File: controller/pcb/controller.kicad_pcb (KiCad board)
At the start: 2 copper layers, 108.1 x 143.5 mm, 75 parts, among them J1 POWER, J2 10K POT, Q1 2N2222, Q10 2N2222, Q11 2N2222, Q12 TIP41, Q13 TIP41, Q14 2N2907, Q15 2N2222, Q2 TIP42, Q3 TIP42, Q4 2N2222, Q5 2N2222, Q6 2N2222, Q7 2N2222, Q8 2N2222, Q9 2N2222, U1 LM78M05_TO220, U2 PIC12F1501-ISN, U3 74HC595

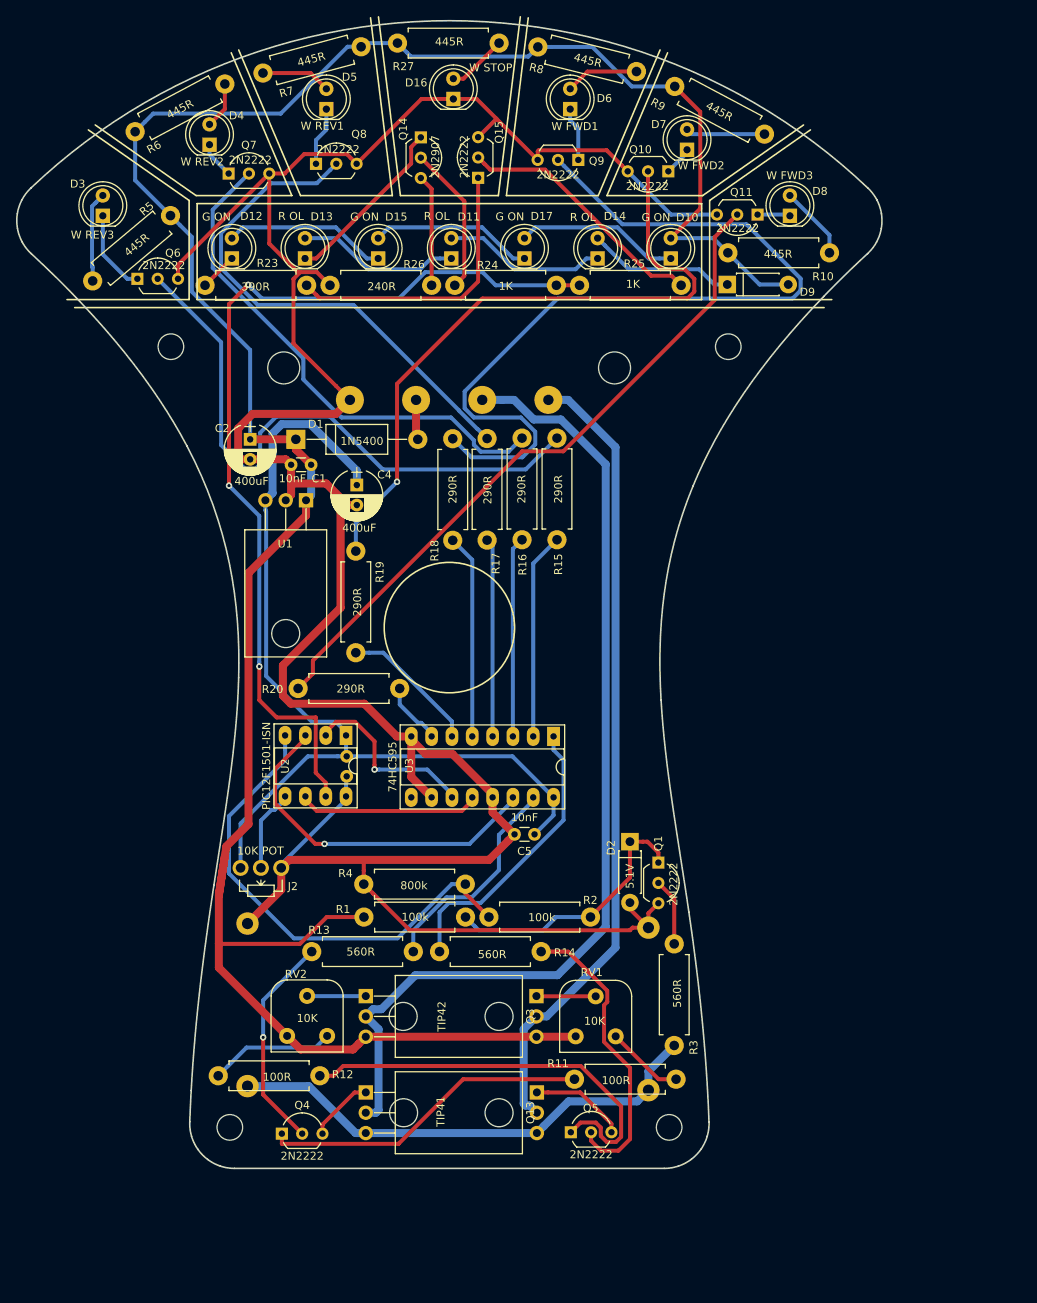
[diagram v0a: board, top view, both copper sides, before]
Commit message: Added gradient control to PCB.
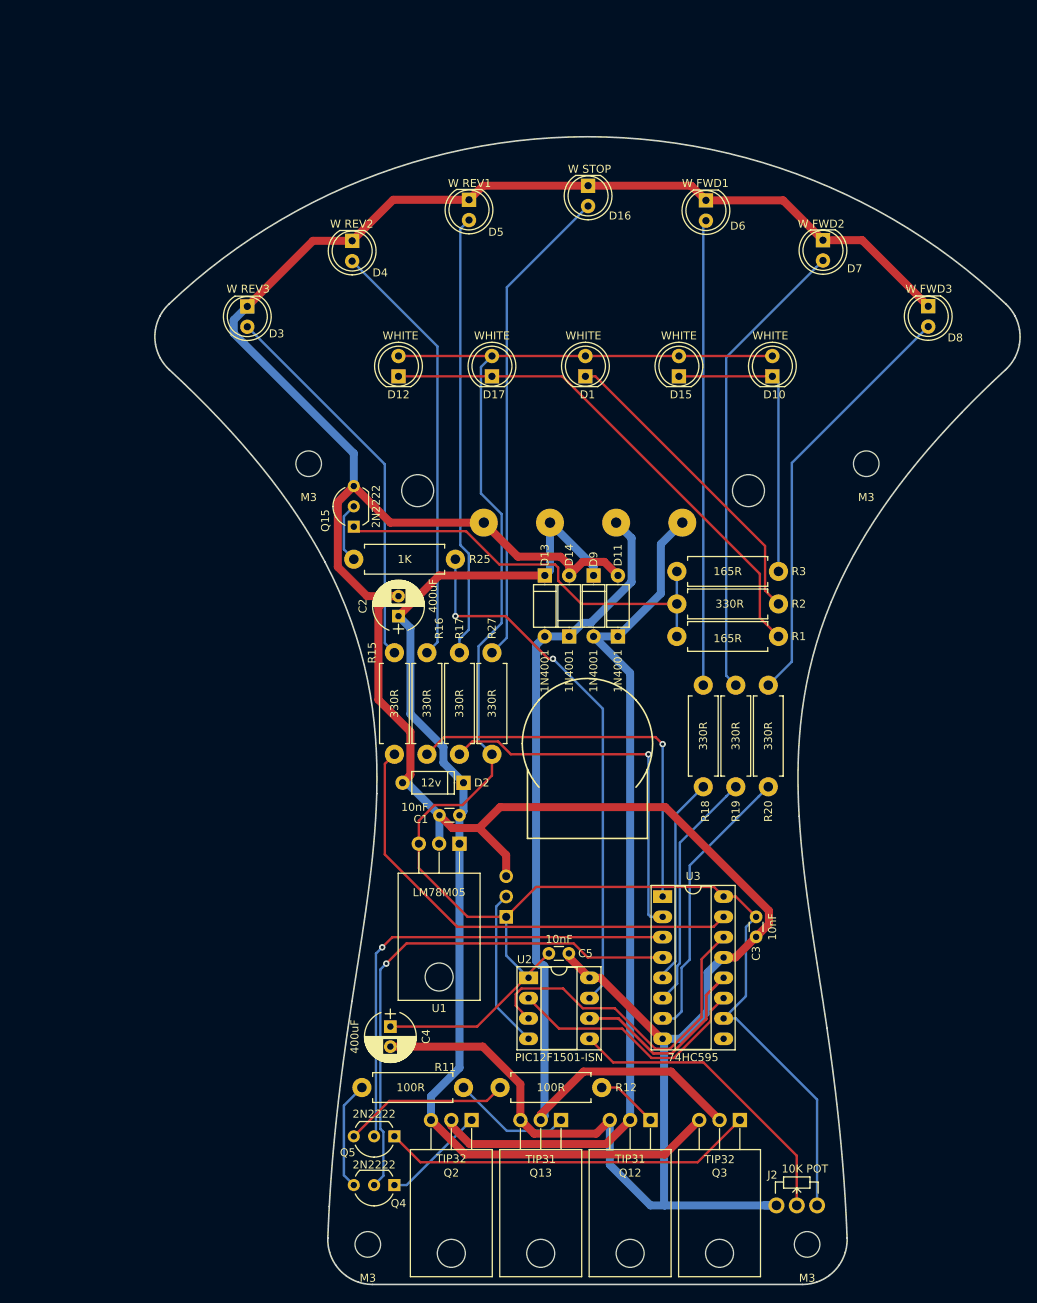
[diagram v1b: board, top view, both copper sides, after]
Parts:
- removed Q1, Q10, Q11, Q6, Q7, Q8, Q9: 2N2222, TO_SOT_Packages_THT:TO-92_Inline_Wide
- removed Q14: 2N2907, TO_SOT_Packages_THT:TO-92_Inline_Wide
- removed R10, R5, R6, R7, R8, R9: 445R, Resistors_THT:R_Axial_DIN0411_L9.9mm_D3.6mm_P12.70mm_Horizontal
- removed R13, R14: 560R, Resistors_THT:R_Axial_DIN0411_L9.9mm_D3.6mm_P12.70mm_Horizontal
- removed R21, R22: 1R, Resistors_THT:R_Axial_DIN0614_L14.3mm_D5.7mm_P20.32mm_Horizontal
- removed R23: 390R, Resistors_THT:R_Axial_DIN0411_L9.9mm_D3.6mm_P12.70mm_Horizontal
- removed R24: 1K, Resistors_THT:R_Axial_DIN0411_L9.9mm_D3.6mm_P12.70mm_Horizontal
- removed R26: 240R, Resistors_THT:R_Axial_DIN0411_L9.9mm_D3.6mm_P12.70mm_Horizontal
- removed R4: 800k, Resistors_THT:R_Axial_DIN0411_L9.9mm_D3.6mm_P12.70mm_Horizontal
- removed the REF** at (101.9, 160.9)
- removed the REF** at (47.0, 160.9)
- removed the REF** at (109.3, 63.3)
- removed the REF** at (39.6, 63.3)
- removed RV1, RV2: 10K, carnivalben:TrimPot_RM065
- added J3: Gradient, Pin_Headers:Pin_Header_Straight_1x03_Pitch2.54mm, B.Cu at (81.5, 134.6)
- added REF**: M3, Mounting_Holes:MountingHole_3.2mm_M3, F.Cu at (119.2, 175.6)
- added REF**: M3, Mounting_Holes:MountingHole_3.2mm_M3, F.Cu at (64.2, 175.6)
- added REF**: M3, Mounting_Holes:MountingHole_3.2mm_M3, F.Cu at (56.8, 78.0)
- added REF**: M3, Mounting_Holes:MountingHole_3.2mm_M3, F.Cu at (126.5, 78.0)
- C3: moved to F.Cu
- D1: value 1N5400 -> WHITE; footprint Diodes_THT:D_DO-15_P15.24mm_Horizontal -> LEDs:LED_D5.0mm
- D10, D12, D15, D17: value G ON -> WHITE
- D11, D13, D14: value R OL -> 1N4001; footprint LEDs:LED_D5.0mm -> Diodes_THT:D_A-405_P7.62mm_Horizontal
- D2: value 5.1V -> 12v; footprint Diodes_THT:D_DO-41_SOD81_P7.62mm_Horizontal -> Diodes_THT:D_A-405_P7.62mm_Horizontal
- D9: value 5.1V -> 1N4001; footprint Diodes_THT:D_DO-41_SOD81_P7.62mm_Horizontal -> Diodes_THT:D_A-405_P7.62mm_Horizontal
- Q12: value TIP41 -> TIP31; moved to F.Cu
- Q13: value TIP41 -> TIP31
- Q2: value TIP42 -> TIP32; moved to F.Cu
- Q3: value TIP42 -> TIP32
- R1: value 100k -> 165R
- R15, R16, R17, R18, R19, R20: value 290R -> 330R
- R2: value 100k -> 330R
- R27: value 445R -> 330R
- R3: value 560R -> 165R
- U1: value LM78M05_TO220 -> LM78M05
- moved R27 76.2 mm to (79.8, 101.6), turned to 270 degrees
- moved J2 74.9 mm to (115.3, 170.7), turned to 90 degrees
- moved C4 67.8 mm to (67.1, 148.3)
- moved R3 60.7 mm to (115.6, 91.4), turned to 180 degrees
- moved R20 58.8 mm to (114.3, 105.7), turned to 270 degrees
- moved C3 55.0 mm to (112.8, 134.6)
- moved R25 53.4 mm to (62.5, 89.9), turned to 0 degrees
- moved R2 53.3 mm to (115.6, 95.5), turned to 180 degrees
- moved R1 52.5 mm to (115.6, 99.6)
- moved D11 51.6 mm to (95.5, 99.6)
- moved R19 50.4 mm to (110.2, 105.7)
- moved D13 49.7 mm to (86.4, 91.9), turned to 270 degrees
- moved Q3 49.3 mm to (110.7, 160.0), turned to 180 degrees
- moved C1 47.6 mm to (75.7, 121.9)
- moved D14 47.4 mm to (89.4, 99.6)
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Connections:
- C1 pad 1: 12vP -> +12V
- C2 pad 1: 12vP -> +12V
- D1 pad 1: 12vP -> Net-(D1-Pad1)
- D1 pad 2: /12v -> 5v
- D10 pad 2: 12vP -> 5v
- D11 pad 1: Net-(D11-Pad1) -> TRACK+
- D11 pad 2: Net-(D11-Pad2) -> GND
- D12 pad 2: Net-(D12-Pad2) -> 5v
- D13 pad 1: Net-(D13-Pad1) -> +12V
- D13 pad 2: Net-(D11-Pad1) -> TRACK-
- D14 pad 1: Net-(D11-Pad2) -> TRACK-
- D14 pad 2: Net-(D14-Pad2) -> GND
- D15 pad 1: Net-(D12-Pad2) -> Net-(D10-Pad1)
- D15 pad 2: Net-(D15-Pad2) -> 5v
- D17 pad 1: Net-(D15-Pad2) -> Net-(D12-Pad1)
- D17 pad 2: Net-(D10-Pad1) -> 5v
- D2 pad 1: Net-(D2-Pad1) -> +12V
- D3 pad 1: Net-(D3-Pad1) -> GND
- D4 pad 1: Net-(D4-Pad1) -> GND
- D5 pad 1: Net-(D5-Pad1) -> GND
- D6 pad 1: Net-(D6-Pad1) -> GND
- D7 pad 1: Net-(D7-Pad1) -> GND
- D8 pad 1: Net-(D8-Pad1) -> GND
- D9 pad 1: Net-(D14-Pad2) -> +12V
- D9 pad 2: 12vP -> TRACK+
- J1 pad 2: /12v -> +12V
- Q12 pad 3: OVERLOAD_DETECT -> GND
- Q13 pad 3: OVERLOAD_DETECT -> GND
- Q2 pad 3: 12vP -> +12V
- Q3 pad 3: 12vP -> +12V
- Q4 pad 1: Net-(Q4-Pad1) -> Net-(Q2-Pad1)
- Q4 pad 3: Net-(Q13-Pad1) -> Net-(Q4-Pad3)
- Q5 pad 1: Net-(Q5-Pad1) -> Net-(Q3-Pad1)
- Q5 pad 3: Net-(Q12-Pad1) -> Net-(Q5-Pad3)
- R1 pad 1: Net-(D2-Pad1) -> Net-(D12-Pad1)
- R1 pad 2: 12vP -> Net-(Q15-Pad1)
- R11 pad 1: Net-(Q4-Pad1) -> Net-(Q13-Pad1)
- R11 pad 2: Net-(R11-Pad2) -> Net-(Q4-Pad3)
- R12 pad 1: Net-(Q5-Pad1) -> Net-(Q12-Pad1)
- R12 pad 2: Net-(R12-Pad2) -> Net-(Q5-Pad3)
- R15 pad 1: Net-(Q6-Pad2) -> Net-(D3-Pad2)
- R16 pad 1: Net-(Q7-Pad2) -> Net-(D4-Pad2)
- R17 pad 1: Net-(Q8-Pad2) -> Net-(D5-Pad2)
- R18 pad 1: Net-(Q9-Pad2) -> Net-(D6-Pad2)
- R19 pad 1: Net-(Q10-Pad2) -> Net-(D7-Pad2)
- R2 pad 1: OVERLOAD -> Net-(D1-Pad1)
- R2 pad 2: Net-(D2-Pad1) -> Net-(Q15-Pad1)
- R20 pad 1: Net-(Q11-Pad2) -> Net-(D8-Pad2)
- R27 pad 2: 12vP -> 5v
- R3 pad 1: OVERLOAD_DETECT -> Net-(D10-Pad1)
- R3 pad 2: Net-(Q1-Pad2) -> Net-(Q15-Pad1)
- U1 pad 1: 12vP -> +12V
- U2 pad 4: OVERLOAD -> Net-(J3-Pad2)
- U3 pad 1: Net-(R14-Pad1) -> Net-(R16-Pad2)
- U3 pad 10: GND -> 5v
- U3 pad 15: Net-(R13-Pad1) -> Net-(R15-Pad2)
- U3 pad 2: Net-(R15-Pad2) -> Net-(R17-Pad2)
- U3 pad 3: Net-(R16-Pad2) -> REV
- U3 pad 4: Net-(R17-Pad2) -> FWD
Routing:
- net 12vP: track 304.6 -> 0.00 mm
- net +12V: track 0.00 -> 141.3 mm
- net 5v: track 117.8 -> 244.1 mm
- net Net-(Q9-Pad2): track 110.9 -> 0.00 mm
- net Net-(Q11-Pad2): track 85.0 -> 0.00 mm
- net Net-(Q10-Pad2): track 84.2 -> 0.00 mm, vias 1 -> 0
- net Net-(Q6-Pad2): track 76.7 -> 0.00 mm
- net Net-(Q8-Pad2): track 64.5 -> 0.00 mm
- net Net-(Q7-Pad2): track 64.4 -> 0.00 mm
- net GND: track 344.2 -> 405.9 mm
- net OVERLOAD_DETECT: track 61.7 -> 0.00 mm
- net OVERLOAD: track 61.2 -> 0.00 mm
- net Net-(D12-Pad1): track 4.74 -> 64.2 mm
- net Net-(D16-Pad2): track 7.56 -> 60.8 mm
- net Net-(Q5-Pad1): track 52.7 -> 0.00 mm
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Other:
- outline, holes or cut-outs redrawn
- net class Default: clearance 0.2 -> 0.25; trace_width 0.25 -> 0.3
- net class High Current added: clearance 0.3, trace_width 1, via_dia 0.8, via_drill 0.4
- rule trace_clearance: 0.2 -> 0.25
- board text added: "Course"
- board text added: "Fine"
- board text removed: "12V"
- board text removed: "GND"
- board text removed: "T+"
- board text removed: "T-"
